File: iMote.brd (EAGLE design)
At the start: 43 x 50 mm, 49 parts, among them CN1 USB-MINIB-UX60SC-MB, CN2 ICSP, CN3 CC-HEADER, IC1 ATmega328P-AU, IC2 FT232RLSSOP, IC3 BLE112-A-VISUAL, Q1 16MHz, T1 2SC1815

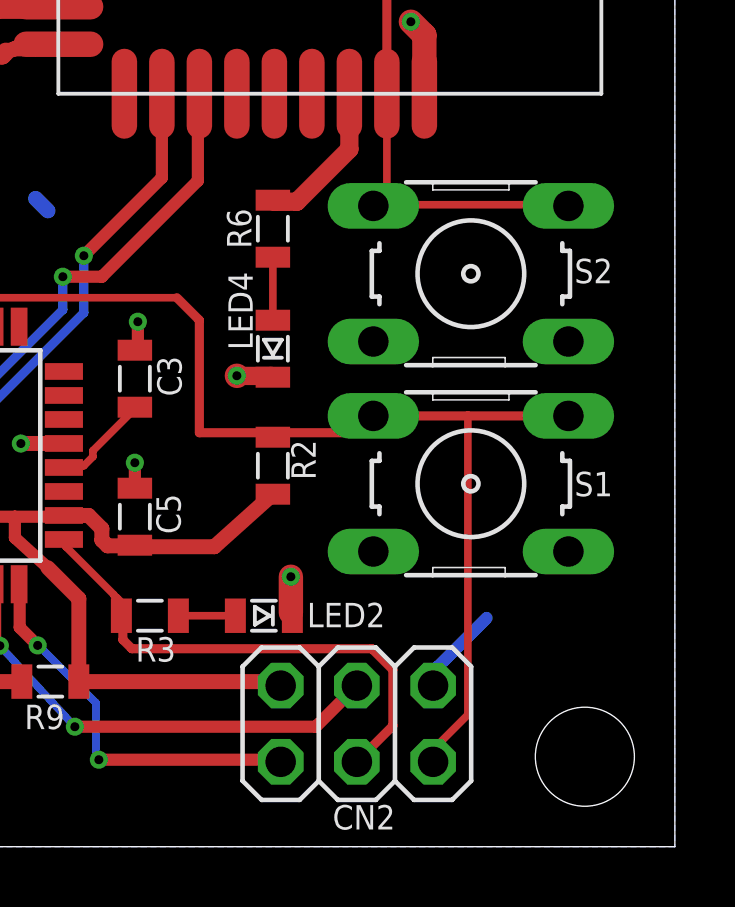
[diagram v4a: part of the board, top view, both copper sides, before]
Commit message: sw1,2をちょい右下へ移動してble112の下の余白を大きく git-revision
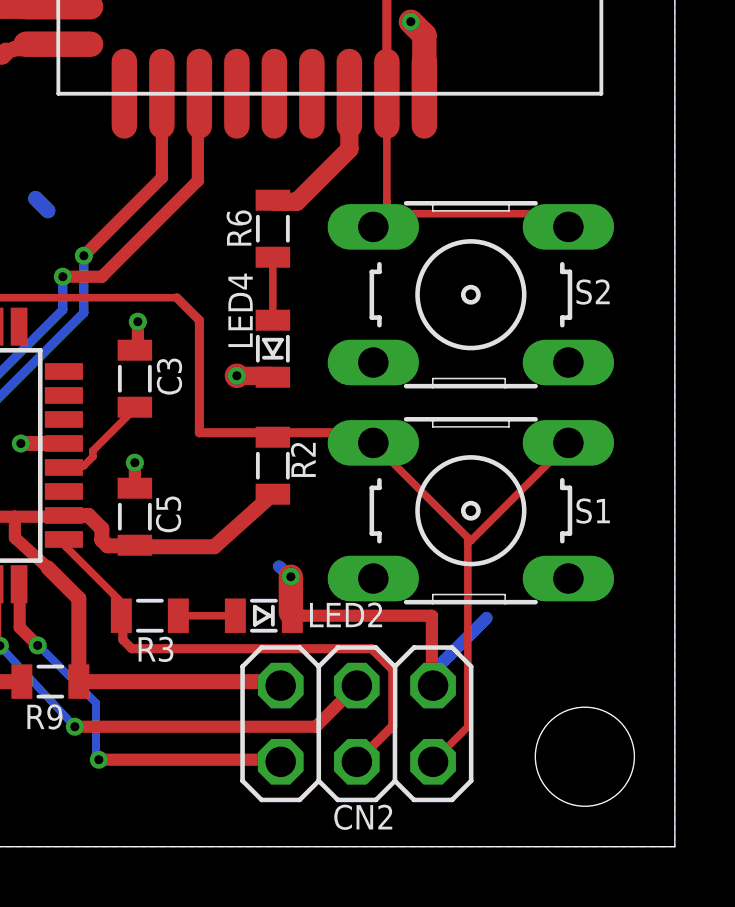
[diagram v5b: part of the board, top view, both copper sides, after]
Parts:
- U$1: value ccb4477 -> 9859471
- moved S1 0.90 mm to (36.2, 11.2)
- moved S2 0.70 mm to (36.2, 18.4)
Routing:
- net GND: track 86.5 -> 94.1 mm
- net !RESET: track 40.1 -> 38.6 mm
- net !BLE/RST: track 50.6 -> 51.6 mm
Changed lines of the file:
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@@
 <wire x1="43" y1="50" x2="0" y2="50" width="0" layer="20"/>
 <wire x1="0" y1="50" x2="0" y2="0" width="0" layer="20"/>
-<rectangle x1="34.5" y1="22.2" x2="39.8" y2="23.2" layer="42"/>
+<rectangle x1="34.5" y1="21.7" x2="39.8" y2="23.2" layer="42"/>
 </plain>
 <attributes>
@@
 <attribute name="VALUE" x="7.386" y="41.238" size="1.27" layer="27" rot="R90"/>
 </element>
-<element name="S1" library="switch-omron" package="B3F-10XX" value="B3F-1000" x="36.2" y="12.1" smashed="yes">
-<attribute name="OC_NEWARK" value="36M3542" x="55.25" y="-9.49" size="1.778" layer="27" display="off"/>
-<attribute name="MPN" value="B3F-1000" x="55.25" y="-9.49" size="1.778" layer="27" display="off"/>
-<attribute name="MF" value="" x="55.25" y="-9.49" size="1.778" layer="27" display="off"/>
-<attribute name="OC_FARNELL" value="176432" x="55.25" y="-9.49" size="1.778" layer="27" display="off"/>
-<attribute name="NAME" x="39.652" y="11.683" size="0.8128" layer="25" ratio="10"/>
-<attribute name="VALUE" x="33.152" y="7.02" size="1.27" layer="27" ratio="10"/>
+<element name="S1" library="switch-omron" package="B3F-10XX" value="B3F-1000" x="36.2" y="11.2" smashed="yes">
+<attribute name="OC_NEWARK" value="36M3542" x="55.25" y="-10.39" size="1.778" layer="27" display="off"/>
+<attribute name="MPN" value="B3F-1000" x="55.25" y="-10.39" size="1.778" layer="27" display="off"/>
+<attribute name="MF" value="" x="55.25" y="-10.39" size="1.778" layer="27" display="off"/>
+<attribute name="OC_FARNELL" value="176432" x="55.25" y="-10.39" size="1.778" layer="27" display="off"/>
+<attribute name="NAME" x="39.652" y="10.783" size="0.8128" layer="25" ratio="10"/>
+<attribute name="VALUE" x="33.152" y="6.12" size="1.27" layer="27" ratio="10"/>
 </element>
 <element name="Q1" library="special" package="QS" value="16MHz" x="7.852" y="10.052" smashed="yes" rot="R90">
@@
 <attribute name="VALUE" x="37.962" y="45.186" size="1.27" layer="27" rot="R180"/>
 </element>
-<element name="S2" library="switch-omron" package="B3F-10XX" value="B3F-1000" x="36.2" y="19.1" smashed="yes">
-<attribute name="OC_NEWARK" value="36M3542" x="16.2" y="29.1" size="1.778" layer="27" display="off"/>
-<attribute name="MPN" value="B3F-1000" x="16.2" y="29.1" size="1.778" layer="27" display="off"/>
-<attribute name="MF" value="" x="16.2" y="29.1" size="1.778" layer="27" display="off"/>
-<attribute name="OC_FARNELL" value="176432" x="16.2" y="29.1" size="1.778" layer="27" display="off"/>
-<attribute name="NAME" x="39.652" y="18.783" size="0.8128" layer="25" ratio="10"/>
-<attribute name="VALUE" x="33.152" y="14.02" size="1.27" layer="27" ratio="10"/>
+<element name="S2" library="switch-omron" package="B3F-10XX" value="B3F-1000" x="36.2" y="18.4" smashed="yes">
+<attribute name="OC_NEWARK" value="36M3542" x="16.2" y="28.4" size="1.778" layer="27" display="off"/>
+<attribute name="MPN" value="B3F-1000" x="16.2" y="28.4" size="1.778" layer="27" display="off"/>
+<attribute name="MF" value="" x="16.2" y="28.4" size="1.778" layer="27" display="off"/>
+<attribute name="OC_FARNELL" value="176432" x="16.2" y="28.4" size="1.778" layer="27" display="off"/>
+<attribute name="NAME" x="39.652" y="18.083" size="0.8128" layer="25" ratio="10"/>
+<attribute name="VALUE" x="33.152" y="13.32" size="1.27" layer="27" ratio="10"/>
 </element>
 <element name="R5" library="my" package="2012" value="330" x="15.9" y="27.3" smashed="yes" rot="R270">
@@
 <attribute name="VALUE" x="9.766" y="45.932" size="1.27" layer="27" rot="R90"/>
 </element>
-<element name="U$1" library="git-revision" package="GIT-REVISION" value="ccb4477" x="0.254" y="-2.448"/>
+<element name="U$1" library="git-revision" package="GIT-REVISION" value="9859471" x="0.254" y="-2.448"/>
 <element name="STANDOFF3" library="SparkFun-Electromechanical" package="STAND-OFF" value="STAND-OFF" x="40" y="47"/>
 <element name="C4" library="my" package="2012" value="0.1uF" x="11.7" y="14.4" smashed="yes" rot="R270">
@@
 <wire x1="17.9" y1="17.4" x2="17.942" y2="17.3346" width="0.254" layer="1"/>
 <wire x1="26.4" y1="18.3" x2="17.9" y2="18.3" width="0.254" layer="1"/>
-<wire x1="36.1" y1="4.4" x2="35.1" y2="3.4" width="0.254" layer="1"/>
-<wire x1="35.1" y1="3.4" x2="34.94" y2="2.83" width="0.254" layer="1"/>
 <wire x1="27.15" y1="13.8" x2="27.15" y2="17.55" width="0.3048" layer="1"/>
 <wire x1="27.15" y1="17.55" x2="26.4" y2="18.3" width="0.3048" layer="1"/>
-<wire x1="32.9488" y1="14.3606" x2="36.1" y2="14.3606" width="0.3048" layer="1"/>
-<wire x1="36.1" y1="14.3606" x2="39.4512" y2="14.3606" width="0.3048" layer="1"/>
 <wire x1="27.15" y1="13.8" x2="29.6" y2="13.8" width="0.3048" layer="1"/>
 <wire x1="29.6" y1="13.8" x2="32.3882" y2="13.8" width="0.3048" layer="1"/>
-<wire x1="32.3882" y1="13.8" x2="32.9488" y2="14.3606" width="0.3048" layer="1"/>
-<wire x1="36.1" y1="14.3606" x2="36.1" y2="4.4" width="0.254" layer="1"/>
+<wire x1="32.3882" y1="13.8" x2="32.9488" y2="13.4606" width="0.3048" layer="1"/>
 <wire x1="29.6" y1="13.65" x2="29.6" y2="13.8" width="0.254" layer="1"/>
+<wire x1="36.1" y1="4" x2="35" y2="2.9" width="0.254" layer="1"/>
+<wire x1="36.1" y1="10.3" x2="36.1" y2="10.2" width="0.254" layer="1"/>
+<wire x1="36.1" y1="10.2" x2="36.1" y2="4" width="0.254" layer="1"/>
+<wire x1="33" y1="13.4" x2="36.1" y2="10.3" width="0.254" layer="1"/>
+<wire x1="35" y1="2.9" x2="34.94" y2="2.83" width="0.254" layer="1"/>
+<wire x1="33" y1="13.4" x2="32.9488" y2="13.4606" width="0.254" layer="1"/>
+<wire x1="36.2" y1="10.2" x2="39.4" y2="13.4" width="0.254" layer="1"/>
+<wire x1="39.4" y1="13.4" x2="39.4512" y2="13.4606" width="0.254" layer="1"/>
+<wire x1="36.2" y1="10.2" x2="36.1" y2="10.2" width="0.254" layer="1"/>
 </signal>
 <signal name="D11/MOSI">
@@
 <wire x1="3.9" y1="38.7" x2="3.864" y2="38.696" width="0.4064" layer="1"/>
 <wire x1="3.9" y1="38.7" x2="3.532" y2="38.7" width="0.4064" layer="1"/>
+<wire x1="30.2" y1="9" x2="29.80414375" y2="9.344228125" width="0.4064" layer="16"/>
+<wire x1="34.9" y1="7.7" x2="30.6" y2="7.7" width="0.4064" layer="1"/>
+<wire x1="34.9" y1="5.4" x2="34.9" y2="7.7" width="0.4064" layer="1"/>
+<wire x1="30.6" y1="7.7" x2="30.2" y2="7.8" width="0.4064" layer="1"/>
+<wire x1="34.9" y1="5.4" x2="34.94" y2="5.37" width="0.4064" layer="1"/>
 </signal>
 <signal name="N$10">
@@
 <contactref element="CN3" pad="7"/>
 <contactref element="S2" pad="2"/>
-<wire x1="33" y1="21.4" x2="32.9488" y2="21.3606" width="0.254" layer="1"/>
 <wire x1="38.1" y1="43.5" x2="38.1" y2="42.9" width="0.254" layer="1"/>
 <wire x1="35.4" y1="46.2" x2="38.1" y2="43.5" width="0.254" layer="1"/>
@@
 <wire x1="38.6" y1="42.9" x2="40.8" y2="41.5" width="0.3048" layer="1"/>
 <wire x1="40.8" y1="41.5" x2="40.8" y2="35.3" width="0.3048" layer="1"/>
-<wire x1="33.1" y1="21.4" x2="39.4" y2="21.4" width="0.254" layer="1"/>
-<wire x1="39.4" y1="21.4" x2="39.4512" y2="21.3606" width="0.254" layer="1"/>
-<wire x1="33.1" y1="21.4" x2="32.9488" y2="21.3606" width="0.254" layer="1"/>
 <wire x1="33.4" y1="21.5" x2="33.4" y2="25.1" width="0.254" layer="1"/>
-<wire x1="33.4" y1="21.5" x2="32.9488" y2="21.3606" width="0.254" layer="1"/>
 <wire x1="33.4" y1="25.2" x2="33.4" y2="25.1" width="0.254" layer="1"/>
 <wire x1="33.4" y1="25.2" x2="33.4" y2="31" width="0.3048" layer="1"/>
@@
 <wire x1="35.3" y1="32.9" x2="38.4" y2="32.9" width="0.3048" layer="1"/>
 <wire x1="38.4" y1="32.9" x2="40.8" y2="35.3" width="0.3048" layer="1"/>
+<wire x1="33.4" y1="21.1" x2="33" y2="20.7" width="0.254" layer="1"/>
+<wire x1="33.4" y1="21.4" x2="33.4" y2="21.1" width="0.254" layer="1"/>
+<wire x1="33" y1="20.7" x2="32.9488" y2="20.6606" width="0.254" layer="1"/>
+<wire x1="33.4" y1="21.4" x2="33.4" y2="21.5" width="0.254" layer="1"/>
+<wire x1="39.4" y1="21.1" x2="33.5" y2="21.1" width="0.254" layer="1"/>
+<wire x1="39.4" y1="20.7" x2="39.4" y2="21.1" width="0.254" layer="1"/>
+<wire x1="33.5" y1="21.1" x2="32.9488" y2="20.6606" width="0.254" layer="1"/>
+<wire x1="39.4" y1="20.7" x2="39.4512" y2="20.6606" width="0.254" layer="1"/>
 </signal>
 <signal name="N$5">

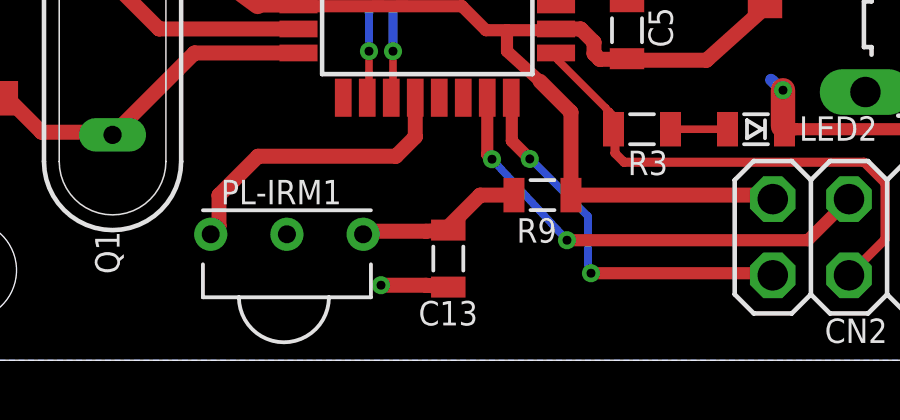
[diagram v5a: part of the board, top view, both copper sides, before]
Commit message: print git revision on board
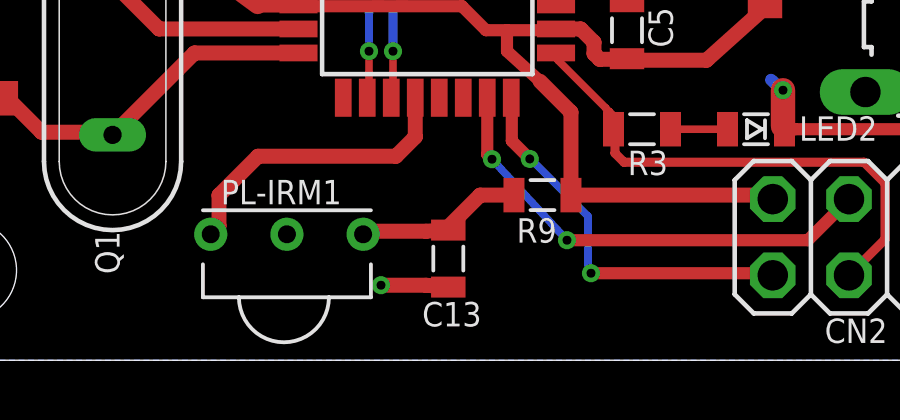
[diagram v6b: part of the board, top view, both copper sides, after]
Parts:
- moved U$1 44.4 mm to (42.5, 11.1), turned to 90 degrees
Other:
- board text added: "IMOTE"
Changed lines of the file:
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@@
 <wire x1="0" y1="50" x2="0" y2="0" width="0" layer="20"/>
 <rectangle x1="34.5" y1="21.7" x2="39.8" y2="23.2" layer="42"/>
+<text x="42.5" y="5.9" size="1" layer="51" font="vector" rot="R90">IMOTE</text>
 </plain>
 <attributes>
@@
 </element>
 <element name="C13" library="my" package="2012" value="4.7uF" x="19.044" y="3.388" smashed="yes" rot="R270">
-<attribute name="NAME" x="18.05" y="1.16" size="0.8128" layer="25"/>
+<attribute name="NAME" x="20.15" y="1.94" size="0.8128" layer="25" rot="R180"/>
 <attribute name="VALUE" x="16.758" y="4.15" size="1.27" layer="27" rot="R270"/>
 </element>
@@
 <attribute name="VALUE" x="9.766" y="45.932" size="1.27" layer="27" rot="R90"/>
 </element>
-<element name="U$1" library="git-revision" package="GIT-REVISION" value="9859471" x="0.254" y="-2.448"/>
+<element name="U$1" library="git-revision" package="GIT-REVISION" value="9859471" x="42.5" y="11.1" smashed="yes" rot="R90">
+<attribute name="VALUE" x="42.5" y="17.99" size="1" layer="51" rot="R90"/>
+</element>
 <element name="STANDOFF3" library="SparkFun-Electromechanical" package="STAND-OFF" value="STAND-OFF" x="40" y="47"/>
 <element name="C4" library="my" package="2012" value="0.1uF" x="11.7" y="14.4" smashed="yes" rot="R270">

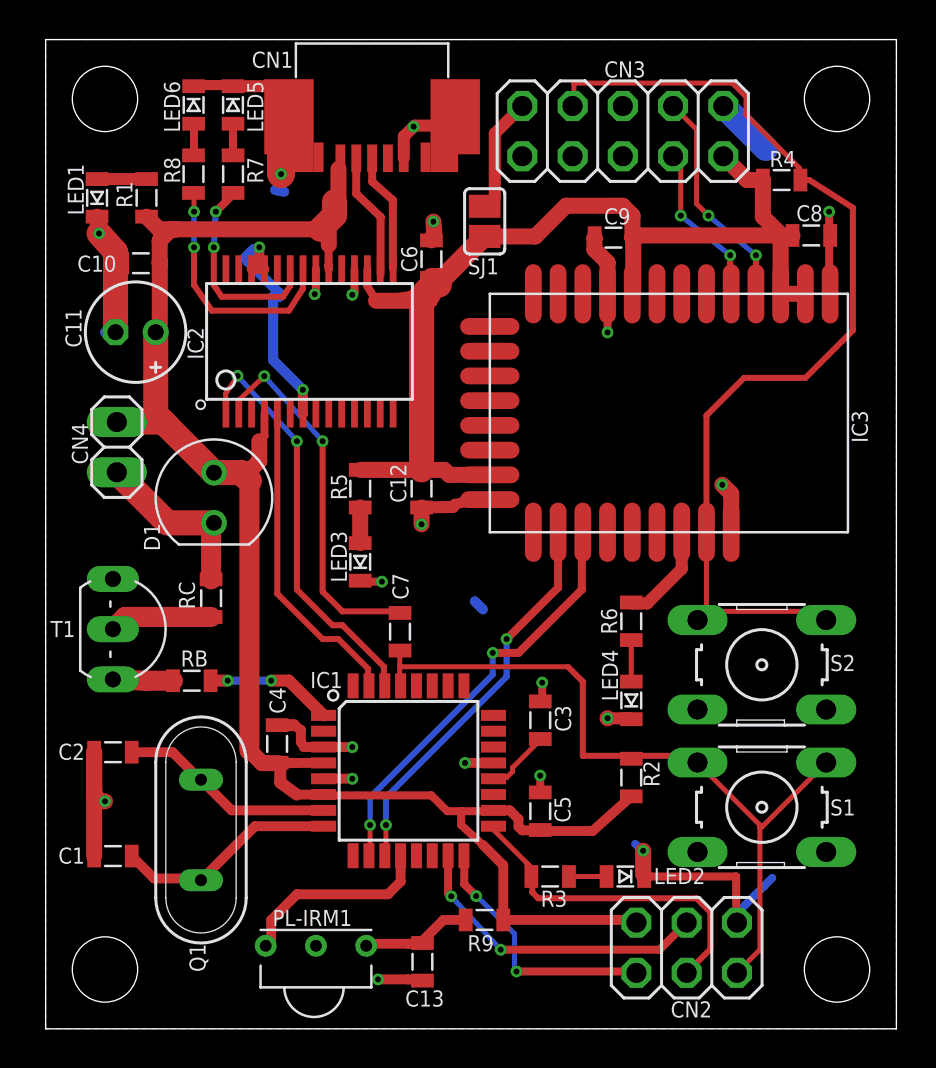
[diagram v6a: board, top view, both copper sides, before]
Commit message: usb-minibコネクタにoverlap警告が出ていたので同じsmdにまとめた
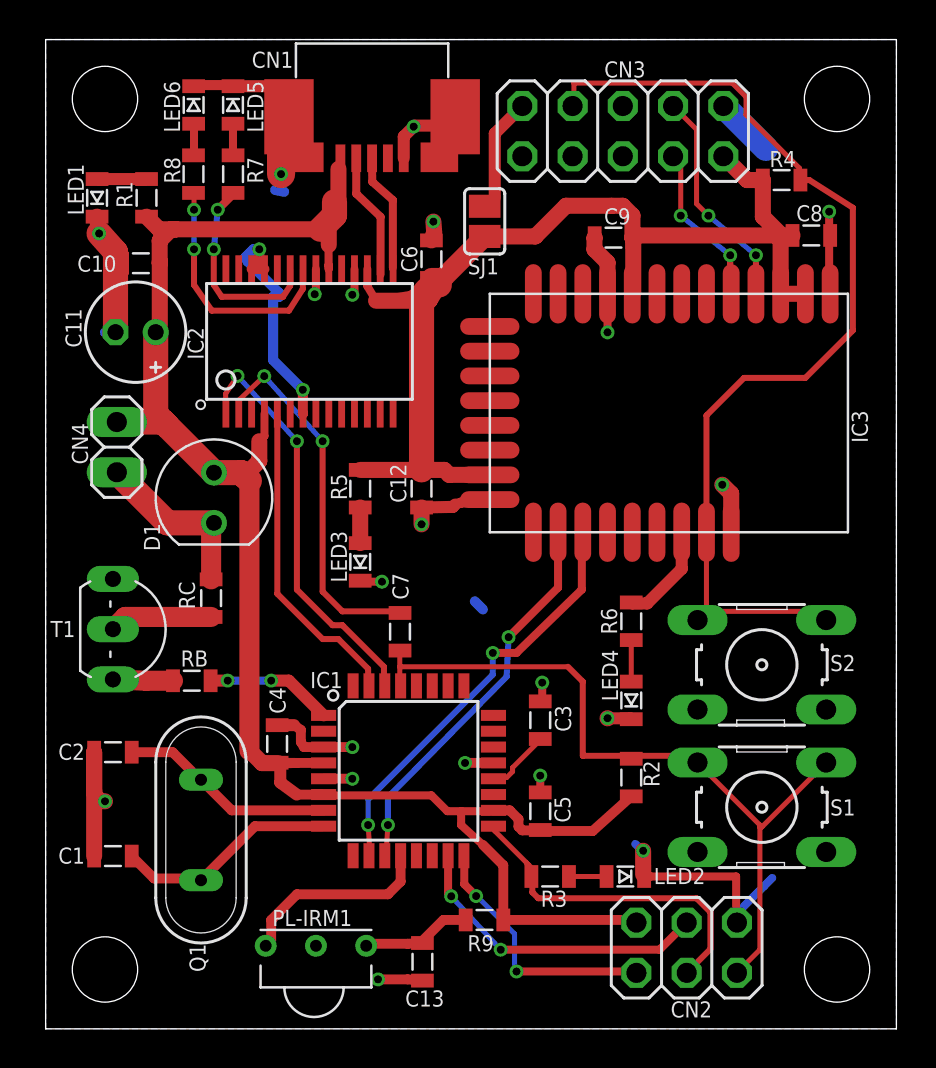
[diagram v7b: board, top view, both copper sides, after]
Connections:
- net GND: now also CN1.S$1@2, CN1.S$1@3, CN1.S$2@2, CN1.S$2@3; no longer CN1.S$3, CN1.S$4

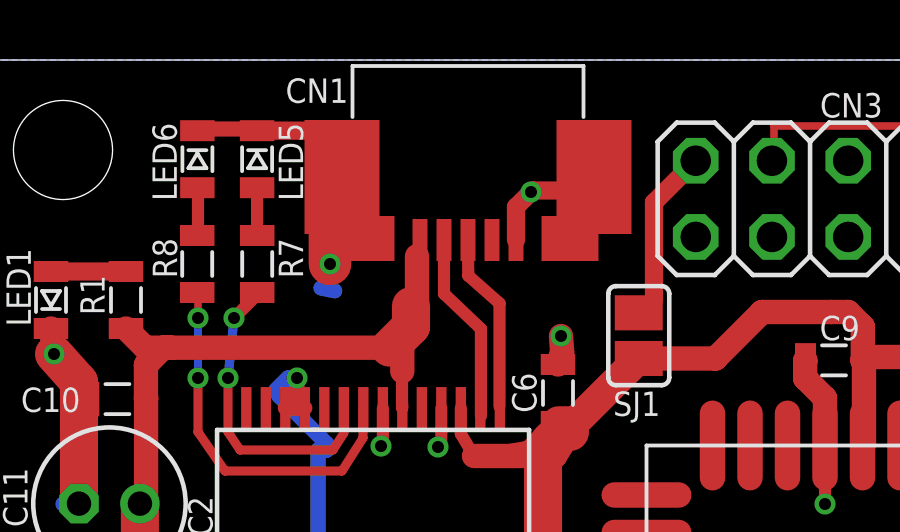
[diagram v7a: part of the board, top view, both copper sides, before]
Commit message: べたgndから0.5mmあける
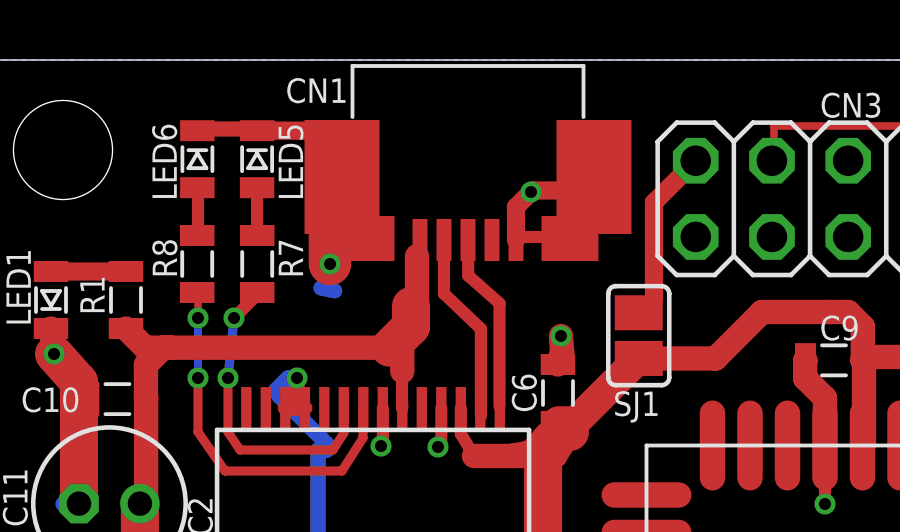
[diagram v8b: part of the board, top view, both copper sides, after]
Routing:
- net GND: track 94.0 -> 98.0 mm
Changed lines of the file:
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@@
 <contactref element="C10" pad="2"/>
 <contactref element="CN1" pad="GND"/>
-<polygon width="1.27" layer="16">
+<polygon width="1.27" layer="16" isolate="0.5">
 <vertex x="0" y="50"/>
 <vertex x="43" y="50"/>
@@
 <wire x1="20.2" y1="46" x2="20.15" y2="45.65" width="0.508" layer="1"/>
 <via x="18.6" y="45.6" extent="1-16" drill="0.4"/>
-<wire x1="18.1" y1="44" x2="18.1" y2="45.1" width="0.6096" layer="1"/>
+<wire x1="18.1" y1="44" x2="18.1" y2="44.1" width="0.6096" layer="1"/>
+<wire x1="18.1" y1="44.1" x2="18.1" y2="45.1" width="0.6096" layer="1"/>
 <wire x1="18.1" y1="45.1" x2="18.6" y2="45.6" width="0.6096" layer="1"/>
 <wire x1="20.15" y1="45.65" x2="18.65" y2="45.65" width="0.6096" layer="1"/>
@@
 <contactref element="CN1" pad="S$1@3"/>
 <contactref element="CN1" pad="S$2@3"/>
+<wire x1="12.6" y1="44.1" x2="13.8" y2="44.1" width="0.4064" layer="1"/>
+<wire x1="13.8" y1="44.1" x2="13.8" y2="44.05" width="0.4064" layer="1"/>
+<wire x1="12.6" y1="44.1" x2="12.85" y2="45.65" width="0.4064" layer="1"/>
+<wire x1="18.4" y1="44.1" x2="19.2" y2="44.1" width="0.4064" layer="1"/>
+<wire x1="19.2" y1="44.1" x2="19.2" y2="44.05" width="0.4064" layer="1"/>
+<wire x1="18.4" y1="44.1" x2="18.1" y2="44.1" width="0.4064" layer="1"/>
 </signal>
 <signal name="N$10">
